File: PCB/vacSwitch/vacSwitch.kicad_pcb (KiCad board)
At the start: 2 copper layers, 91.2 x 50.8 mm, 28 parts, among them J1 Mains, J2 RS232, J3 ISP, J4 VoltFreeContact, K1 HE721A0510, Q1 BC547, U1 ATtiny85-20PU, U2 ACS712xLCTR-20A, U3 MOC3043M

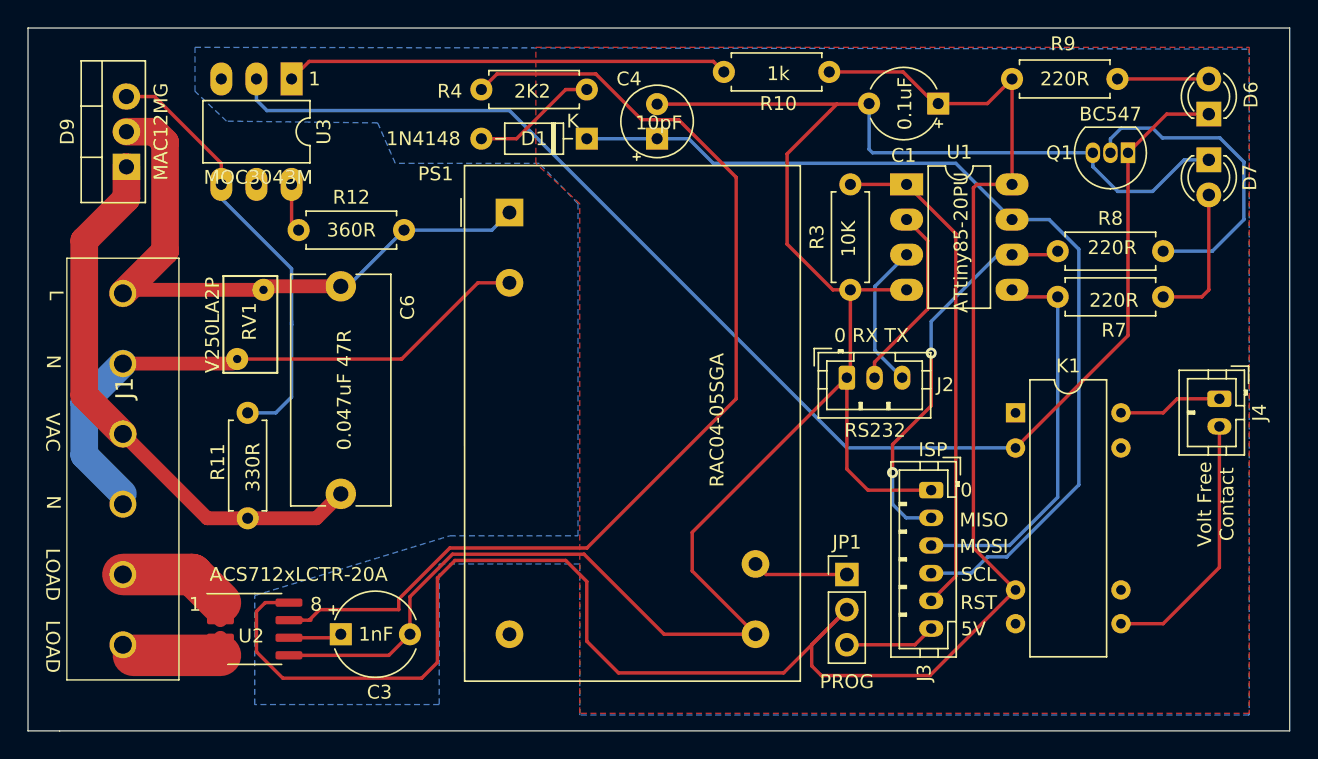
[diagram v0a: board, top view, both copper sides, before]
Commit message: update PCB (errors fixed)
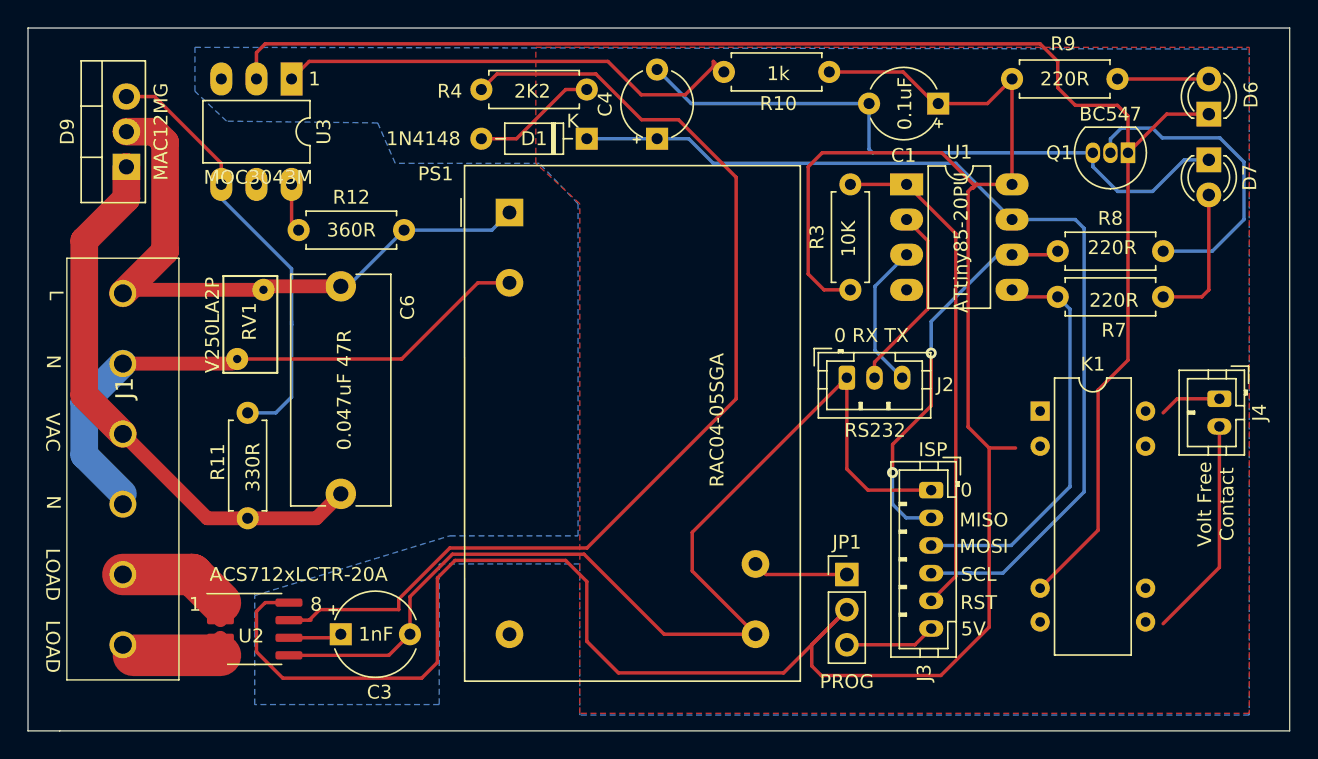
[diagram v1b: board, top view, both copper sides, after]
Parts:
- C4: footprint Capacitor_THT:CP_Radial_Tantal_D5.0mm_P2.50mm -> Capacitor_THT:CP_Radial_Tantal_D5.0mm_P5.00mm
- moved K1 1.78 mm to (177.5, 105.2)
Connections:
- K1 pad 2: Net-(D6-Pad1) -> VCC
- K1 pad 6: VCC -> Net-(D6-Pad1)
- R3 pad 2: 0V -> VCC
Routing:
- net 0V: track 153.2 -> 126.5 mm
- net VCC: track 142.4 -> 168.4 mm
- net Net-(D6-Pad1): track 98.5 -> 112.2 mm
- net SW1: track 19.0 -> 15.9 mm
- net SW2: track 7.53 -> 4.48 mm
- net SCL: track 69.2 -> 71.6 mm
- net Net-(R10-Pad2): track 32.1 -> 34.3 mm
- net MOSI: track 28.6 -> 29.4 mm
